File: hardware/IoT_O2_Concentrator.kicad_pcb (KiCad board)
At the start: 2 copper layers, 72.1 x 77 mm, 20 parts, among them J1 5V_BUCK_OUT, J10 12V_BUCK_IN, J11 O2_VCC_SEL, J12 BOX_SWITCH, J13 DC_MODULE, J2 BUZZER, J3 O2_SENSOR, J4 GPIOs, J5 RELAY, J6 LCD_20x04, J7 SIM_GSM_EVB, J8 POTENTIOMETER, J9 GPIO_SUPPLY

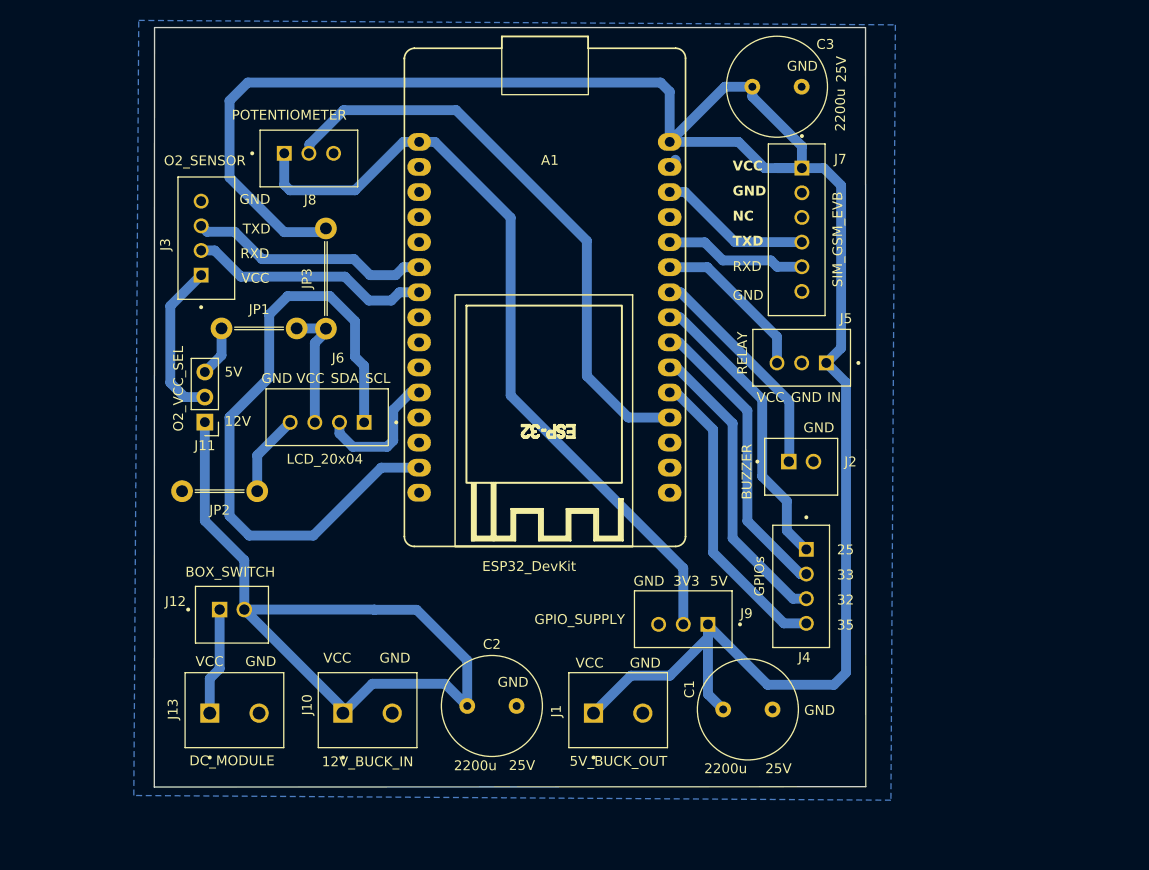
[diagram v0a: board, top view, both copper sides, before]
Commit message: Hardware v2.0: bare SIM800 module support and routing cleanup
Add JST for bare SIM module with 1N4001 drop from 5 V; remove O2 sensor voltage selector (sensor accepts 5 V). Replace routing jumpers with net ties (GND only) for DRC continuity; sheet version set to 2.0.
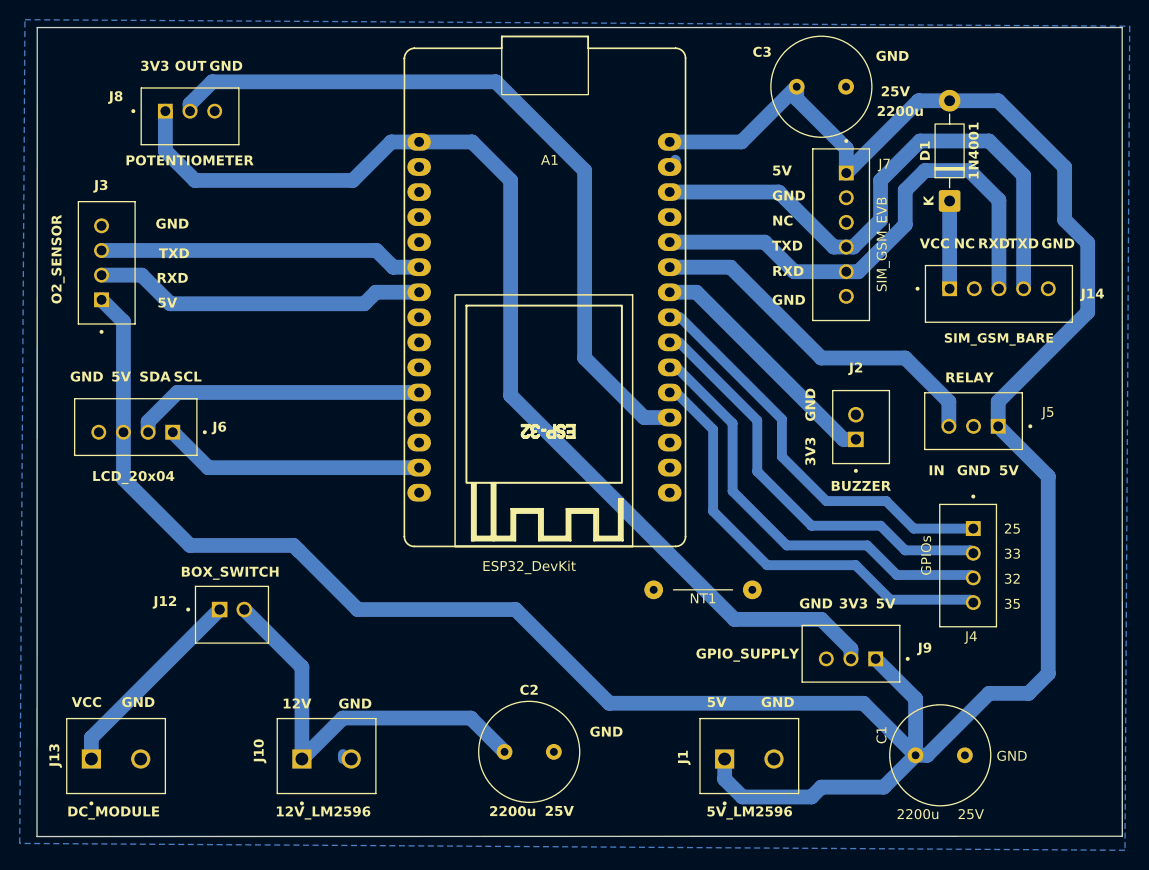
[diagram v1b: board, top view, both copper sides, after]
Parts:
- removed J11: O2_VCC_SEL, Connector_PinHeader_2.54mm:PinHeader_1x03_P2.54mm_Vertical
- removed JP1: 5V_JUMPER, PCM_Jumper_AKL:Jumper_P7.62mm_D1.2mm
- removed JP2: GND_JUMPER, PCM_Jumper_AKL:Jumper_P7.62mm_D1.2mm
- removed JP3: 5V_JUMPER, PCM_Jumper_AKL:Jumper_P10.16mm_D1.2mm
- added D1: 1N4001, Diode_THT:D_DO-41_SOD81_P10.16mm_Horizontal, F.Cu at (196.5, 57.6)
- added J14: SIM_GSM_BARE, footprint:JST_B5B-XH-A, F.Cu at (201.5, 67.0)
- added NT1: NetTie_2, PCM_SL_Jumpers:JUP_P10mm, F.Cu at (171.5, 97.0)
- J1: value 5V_BUCK_OUT -> 5V_LM2596
- J10: value 12V_BUCK_IN -> 12V_LM2596
- moved C1 20.0 mm to (193.1, 113.8)
- moved J6 19.4 mm to (114.0, 80.5)
- moved J5 18.6 mm to (198.9, 79.9)
- moved J9 17.4 mm to (186.5, 103.5)
- moved J4 17.1 mm to (198.4, 94.5)
- moved J1 14.1 mm to (173.7, 114.2)
- moved J13 12.9 mm to (109.5, 114.2)
- moved J8 12.8 mm to (119.5, 49.0)
- moved J3 10.4 mm to (111.1, 63.9)
- moved J2 7.29 mm to (187.5, 80.5), turned to -90 degrees
- moved J10 6.24 mm to (130.8, 114.2)
- moved C2 5.99 mm to (151.4, 113.4)
- moved J7 4.53 mm to (185.5, 61.0)
- moved C3 4.50 mm to (181.0, 46.0)
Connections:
- J3 pad 1: /O2_VCC -> /5V_VCC
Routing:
- net /5V_VCC: track 225.0 -> 275.4 mm
- net /SIM_TXD: track 15.5 -> 57.9 mm
- net /SCL_22: track 66.1 -> 26.5 mm
- net /12V_VCC: track 79.4 -> 41.2 mm
- net /SIM_RXD: track 14.4 -> 51.1 mm
- net /3V3_VCC: track 80.1 -> 111.4 mm
- net /RELAY_27: track 16.4 -> 36.4 mm
- net /O2_VCC: track 16.3 -> 0.00 mm
- net /SDA_21: track 13.9 -> 29.8 mm
- net /POT_34: track 59.8 -> 75.5 mm
- net /GPIO35: track 30.9 -> 44.4 mm
- net /GPIO32: track 30.4 -> 43.6 mm
- net /GPIO33: track 30.1 -> 42.7 mm
- net /GPIO25: track 29.9 -> 41.9 mm
- net /12V_RAW: track 10.8 -> 20.5 mm
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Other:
- board size 72.1 x 77 mm -> 110 x 82 mm
- board text added: "OUT"

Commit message: Board V2 and firmware V2 implemented with softAP
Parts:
- added NT2: NetTie_2, PCM_SL_Jumpers:JUP_P10mm, F.Cu at (166.3, 109.9)
- J1: value 5V_LM2596 -> LM2596_OUT
- J10: value 12V_LM2596 -> LM2596_IN
- moved C3 5.38 mm to (186.4, 45.8), turned to 180 degrees
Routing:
- net /5V_VCC: track 275.4 -> 289.8 mm
